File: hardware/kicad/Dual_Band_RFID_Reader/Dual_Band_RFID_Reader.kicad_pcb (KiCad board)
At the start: 2 copper layers, 74 x 74 mm, 50 parts, among them Q1 BC517, U1 Adafruit_Huzzah32, U2 LM393, U3 LM324, U4 MFRC522, Y1 Crystal

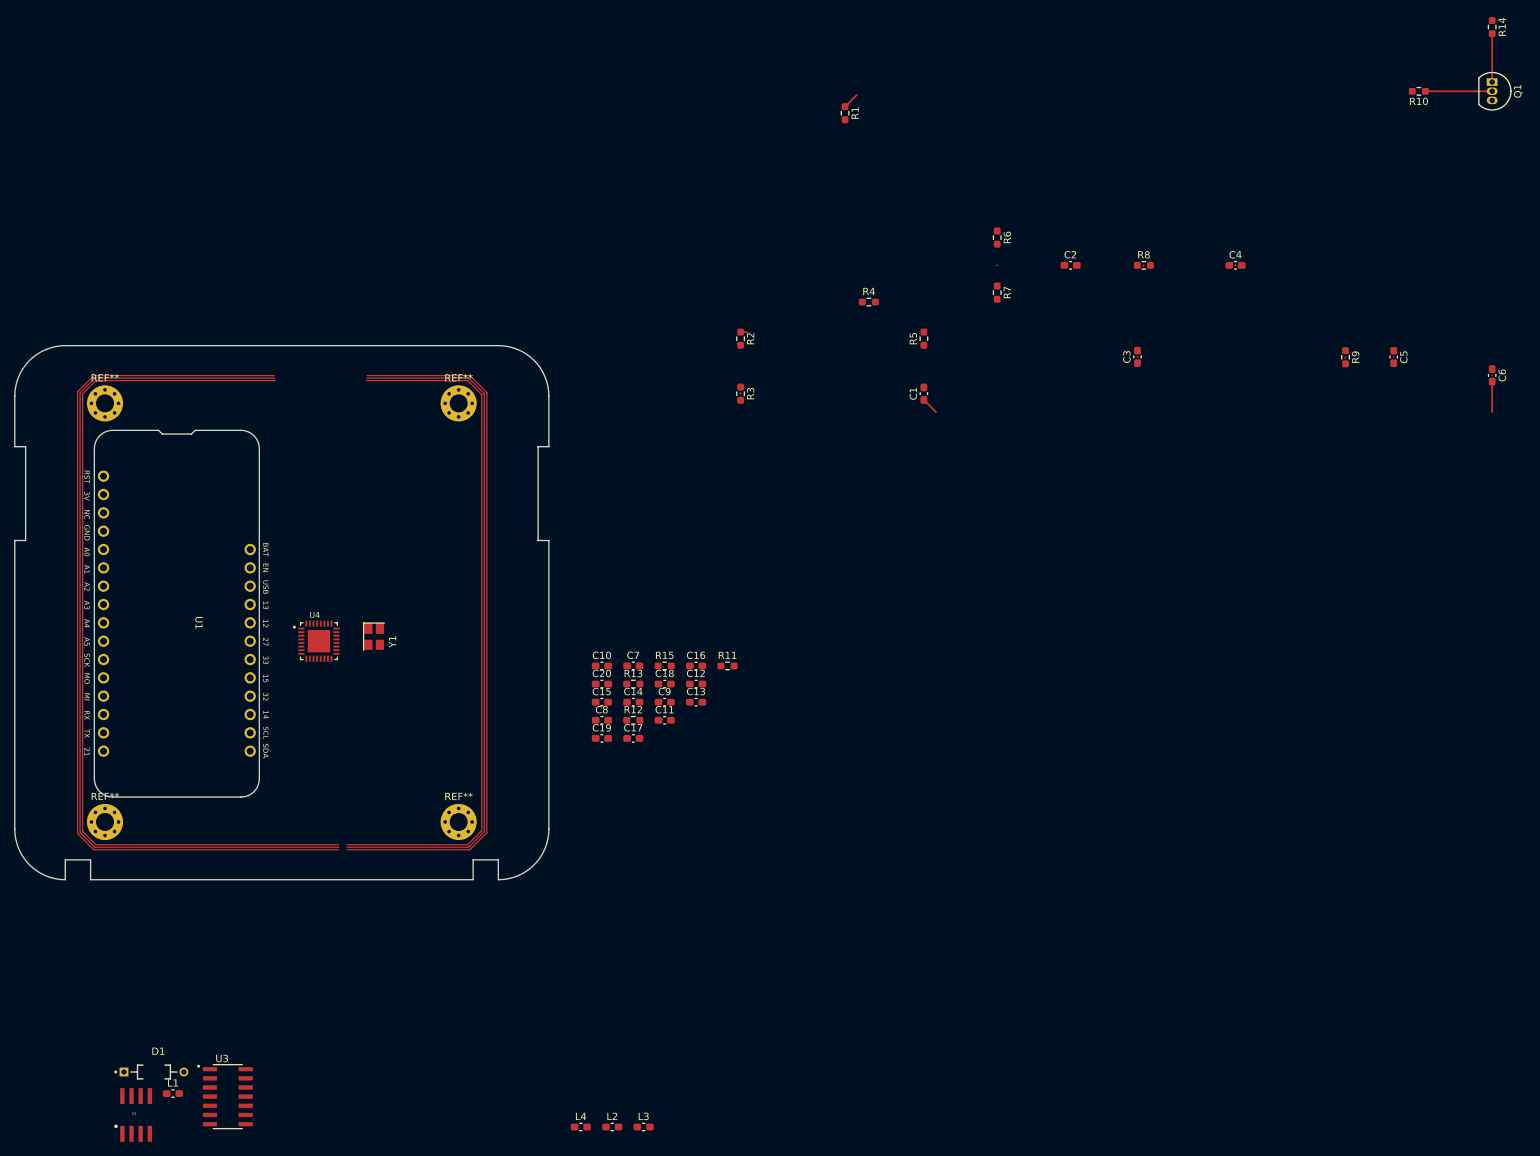
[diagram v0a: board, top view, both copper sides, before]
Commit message: Board Layout WIP
* Added correct footprint for the components that were
  producing errors
* added HF antenna trace on board periphery
* added pads for the LF antenna coil to be connected later
* corrected all the DRC errors
* completed HF layout
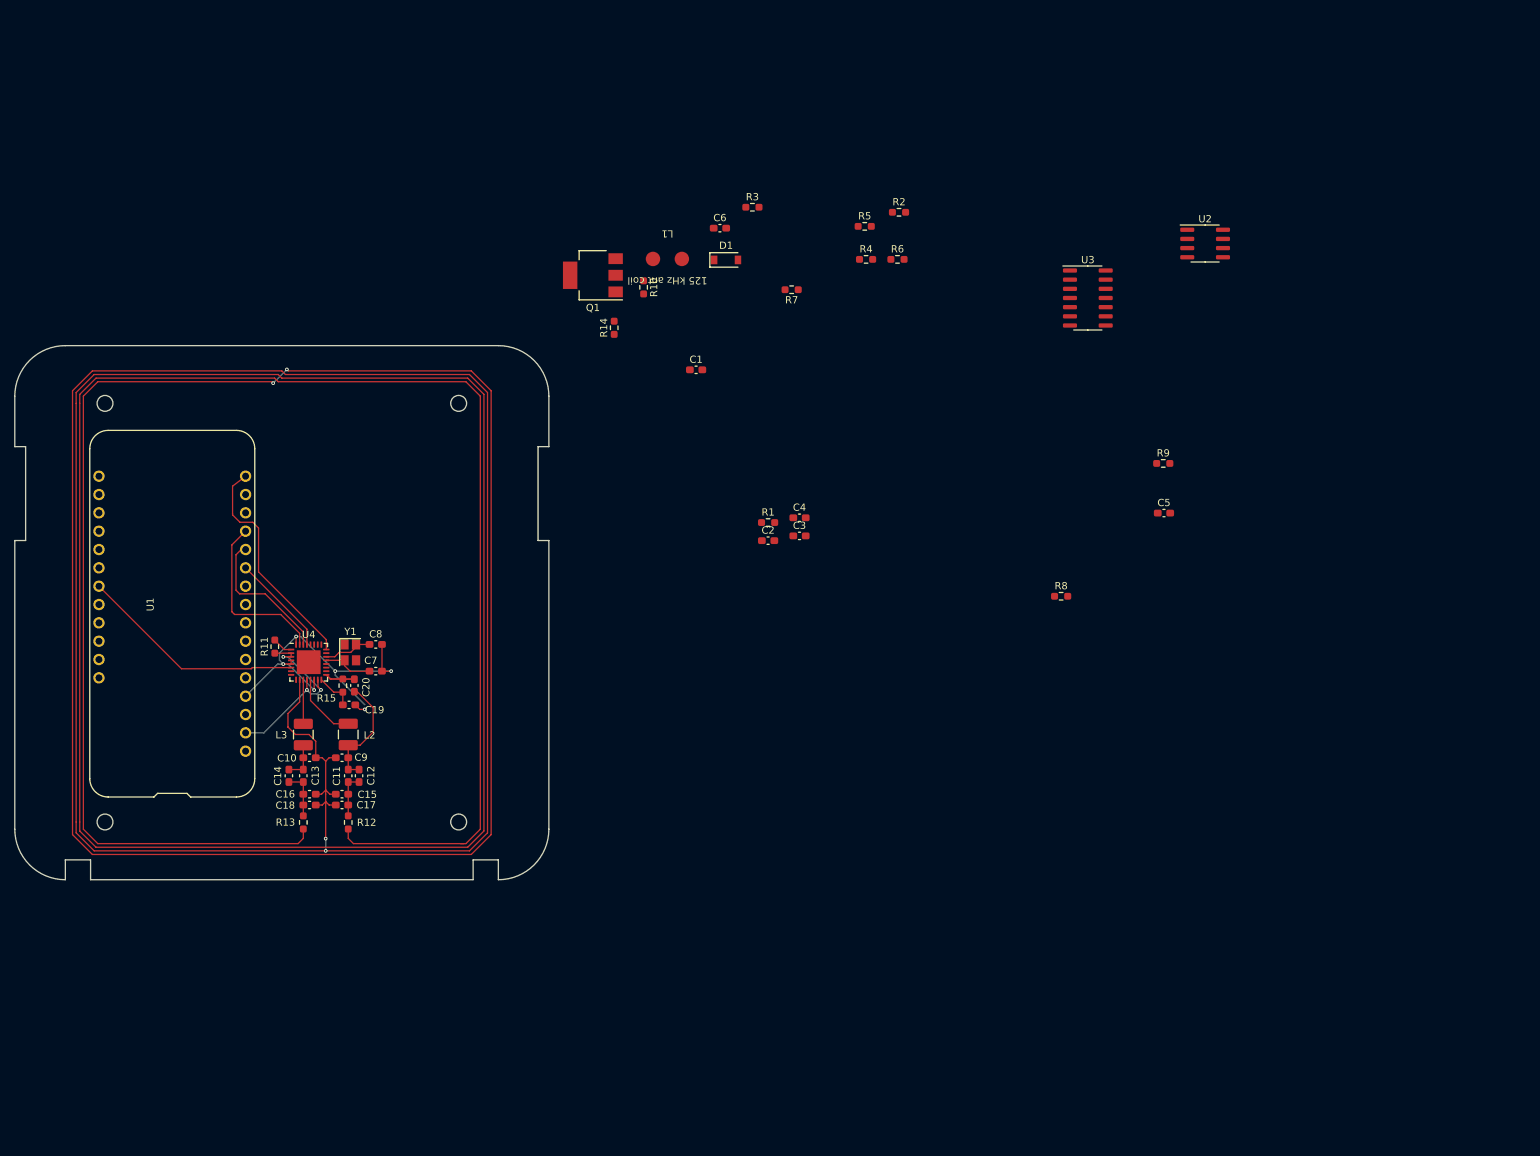
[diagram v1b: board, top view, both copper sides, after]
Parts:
- removed L4: INDUCTOR, Inductor_SMD:L_0603_1608Metric_Pad1.05x0.95mm_HandSolder
- removed the REF** at (123.5, 75.0)
- removed the REF** at (74.5, 133.0)
- removed the REF** at (123.5, 133.0)
- removed the REF** at (74.5, 75.0)
- added REF**: MountingHole_2.2mm_M2, MountingHole:MountingHole_2.2mm_M2, F.Cu at (74.5, 133.0)
- added REF**: MountingHole_2.2mm_M2, MountingHole:MountingHole_2.2mm_M2, F.Cu at (123.5, 75.0)
- added REF**: MountingHole_2.2mm_M2, MountingHole:MountingHole_2.2mm_M2, F.Cu at (123.5, 133.0)
- added REF**: MountingHole_2.2mm_M2, MountingHole:MountingHole_2.2mm_M2, F.Cu at (74.5, 75.0)
- D1: footprint ZenerDiodes:DIOAD829W49L456D191 -> Diode_SMD:D_SOD-123
- L1: footprint Inductor_SMD:L_0603_1608Metric_Pad1.05x0.95mm_HandSolder -> Capstone Footprint Lib:LF Antenna Pads
- L2, L3: footprint Inductor_SMD:L_0603_1608Metric_Pad1.05x0.95mm_HandSolder -> Inductor_SMD:L_1210_3225Metric_Pad1.42x2.65mm_HandSolder
- Q1: footprint Package_TO_SOT_THT:TO-92_Inline -> Package_TO_SOT_SMD:SOT-223
- U1: footprint Footprint Library:Adafruit Feather Huzzah 32 -> Capstone Footprint Lib:Adafruit Feather Huzzah 32
- U2: footprint DualComparator_LM393:SO08 -> Package_SO:SOIC-8_3.9x4.9mm_P1.27mm
- U3: footprint GPOPAmp_LM324:SOIC127P600X175-14N -> Package_SO:SOIC-14_3.9x8.7mm_P1.27mm
- U4: footprint MIFARE:QFN50P500X500X100-33N -> Package_DFN_QFN:QFN-32-1EP_5x5mm_P0.5mm_EP3.3x3.3mm
- Y1: footprint Footprint Library:Crystal_SMD_3225-4Pin_3.2x2.5mm_HandSoldering -> Capstone Footprint Lib:Crystal_SMD_3225-4Pin_3.2x2.5mm_HandSoldering
- moved U2 191.1 mm to (226.9, 52.9)
- moved U3 162.6 mm to (210.7, 60.4)
- moved D1 137.6 mm to (160.6, 55.1)
- moved L1 137.0 mm to (152.4, 52.0), turned to 180 degrees
- moved R14 128.6 mm to (145.1, 64.5), turned to 90 degrees
- moved Q1 127.4 mm to (142.1, 57.2), turned to 180 degrees
- moved R10 110.8 mm to (149.1, 58.9), turned to -90 degrees
- moved C6 108.9 mm to (159.7, 50.7), turned to 0 degrees
- moved L3 72.0 mm to (102.0, 120.9), turned to -90 degrees
- moved C4 69.8 mm to (170.7, 90.8)
- moved L2 65.5 mm to (108.2, 120.9), turned to -90 degrees
- moved R11 62.8 mm to (98.0, 108.7), turned to 90 degrees
- moved R1 57.7 mm to (166.4, 91.5), turned to 0 degrees
- moved C13 57.3 mm to (100.0, 126.6), turned to 90 degrees
- moved C2 56.7 mm to (166.4, 94.0)
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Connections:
- L2 pad 1: Net-(U4-TX1) -> Net-(U4-TX2)
- L3 pad 1: Net-(U4-TX2) -> Net-(U4-TX1)
- R12 pad 1: Net-(L4-Pad1) -> Net-(U4-TVSS)
- R13 pad 1: Net-(L4-Pad2) -> Net-(U4-TVSS)
- U1 pad 11: (no net) -> /High Frequency RF/SCK
- U1 pad 12: (no net) -> /High Frequency RF/MOSI
- U1 pad 13: (no net) -> /High Frequency RF/MISO
- U1 pad 14: (no net) -> /Low Frequency RF/LF_RF_RX
- U1 pad 15: (no net) -> /Low Frequency RF/LF_RF_TX
- U1 pad 16: (no net) -> /High Frequency RF/CS
- U1 pad 2: (no net) -> +3V3
- U1 pad 4: /IRQ -> GND
- U1 pad 5: /High Frequency RF/SCK -> (no net)
- Y1 pad 2: Net-(U4-OSCIN) -> (no net)
- Y1 pad 3: (no net) -> Net-(U4-OSCIN)
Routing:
- net Net-(U4-TVSS): track 0.00 -> 988.9 mm, vias 0 -> 4
- net /High Frequency RF/SCK: track 376.2 -> 14.2 mm
- net (no net): track 293.6 -> 0.00 mm
- net GND: track 6.92 -> 50.0 mm, vias 0 -> 6
- net /High Frequency RF/RST: track 0.00 -> 31.4 mm
- net /High Frequency RF/CS: track 0.00 -> 31.3 mm
- net /High Frequency RF/MISO: track 0.00 -> 24.1 mm
- net +3V3: track 3.21 -> 27.3 mm, vias 0 -> 3
- net /High Frequency RF/MOSI: track 0.00 -> 20.0 mm
- net Net-(C11-Pad2): track 0.00 -> 15.9 mm
- net Net-(U4-TX2): track 0.00 -> 9.43 mm
- net Net-(Q1-B): track 9.25 -> 0.00 mm
- net Net-(U4-OSCIN): track 0.00 -> 7.04 mm
- net Net-(U4-OSCOUT): track 0.00 -> 6.91 mm
- net Net-(Q1-C): track 6.71 -> 0.00 mm
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
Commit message: Updates traces
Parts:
- moved U2 117.0 mm to (119.9, 100.1), turned to 90 degrees
- moved C5 113.0 mm to (108.2, 88.6)
- moved R9 113.0 mm to (108.2, 86.8)
- moved U3 111.9 mm to (118.9, 124.5)
- moved R8 106.9 mm to (102.1, 80.9), turned to -90 degrees
- moved R6 91.6 mm to (116.8, 117.0), turned to 180 degrees
- moved R5 87.3 mm to (121.4, 115.5)
- moved R2 85.6 mm to (110.7, 91.9), turned to 180 degrees
- moved R4 85.2 mm to (121.4, 117.0)
- moved R7 77.1 mm to (116.8, 115.5)
- moved C4 68.9 mm to (102.1, 84.4), turned to -90 degrees
- moved R3 68.4 mm to (110.7, 90.4)
- moved C6 65.9 mm to (105.7, 88.4), turned to 90 degrees
- moved D1 64.4 mm to (107.7, 91.9), turned to 90 degrees
- moved C2 63.6 mm to (104.1, 80.9), turned to 90 degrees
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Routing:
- net /Low Frequency RF/LF_RF_RX: track 0.00 -> 78.3 mm, vias 0 -> 1
- net Net-(U3A-+): track 0.00 -> 56.9 mm, vias 0 -> 2
- net +3V3: track 27.3 -> 80.2 mm, vias 3 -> 10
- net GND: track 50.0 -> 98.4 mm
- net +5V: track 0.00 -> 39.4 mm, vias 0 -> 1
- net Net-(D1-K): track 0.00 -> 31.4 mm
- net Net-(U2A-+): track 0.00 -> 30.2 mm
- net Net-(C2-Pad2): track 0.00 -> 26.0 mm, vias 0 -> 2
- net Net-(U2A--): track 0.00 -> 23.3 mm
- net /Low Frequency RF/LF_RF_TX: track 0.00 -> 18.2 mm
- net Net-(U3A--): track 0.00 -> 9.97 mm
- net Net-(D1-A): track 0.00 -> 9.69 mm
- net Net-(Q1-C): track 0.00 -> 7.62 mm, vias 0 -> 2
- net Net-(Q1-B): track 0.00 -> 5.63 mm
- net Net-(Q1-E): track 0.00 -> 5.17 mm
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
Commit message: Updates traces_1
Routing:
- net GND: track 98.4 -> 103.3 mm
- net Net-(U2A--): track 23.3 -> 24.8 mm
- net +3V3: track 80.2 -> 81.4 mm
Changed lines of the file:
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@@
   (segment (start 112.875 112.1) (end 114.15 112.1) (width 0.1524) (layer "F.Cu") (net 1))
   (segment (start 109.8 117.4) (end 109.175 116.775) (width 0.1524) (layer "F.Cu") (net 1))
+  (segment (start 110.458987 88.614987) (end 109.066499 88.614987) (width 0.1524) (layer "F.Cu") (net 1))
   (segment (start 113.2905 108.8155) (end 112.875 108.4) (width 0.1524) (layer "F.Cu") (net 1))
   (segment (start 106.46352 90.71552) (end 106.46352 88.17552) (width 0.1524) (layer "F.Cu") (net 1))
@@
   (segment (start 109.0665 104.5915) (end 109.0665 95.504) (width 0.152) (layer "F.Cu") (net 1))
   (segment (start 115.9275 113.3875) (end 115.9275 115.470874) (width 0.1524) (layer "F.Cu") (net 1))
+  (segment (start 111.6565 89.8125) (end 110.458987 88.614987) (width 0.1524) (layer "F.Cu") (net 1))
   (segment (start 114.322711 110.213289) (end 114.15 110.386) (width 0.1524) (layer "F.Cu") (net 1))
   (segment (start 100.975 107.3) (end 100.975 108.4225) (width 0.1524) (layer "F.Cu") (net 1))
+  (segment (start 111.6565 90.424) (end 111.6565 89.8125) (width 0.1524) (layer "F.Cu") (net 1))
   (segment (start 111.252 90.424) (end 111.6565 90.424) (width 0.25) (layer "F.Cu") (net 1))
   (segment (start 100.2875 111.11) (end 99.215 111.11) (width 0.1524) (layer "F.Cu") (net 1))
@@
   (segment (start 103.475 113.2975) (end 103.475 114.725) (width 0.1524) (layer "F.Cu") (net 1))
   (segment (start 119.379999 113.942401) (end 120.5495 113.942401) (width 0.1524) (layer "F.Cu") (net 1))
+  (segment (start 106.4 112.1) (end 105.1725 112.1) (width 0.1524) (layer "F.Cu") (net 1))
   (segment (start 99.215 111.11) (end 99.2 111.125) (width 0.1524) (layer "F.Cu") (net 1))
   (segment (start 105.8175 87.5295) (end 105.664 87.5295) (width 0.25) (layer "F.Cu") (net 1))
@@
   (segment (start 108.712 91.44) (end 108.712 89.614978) (width 0.1524) (layer "F.Cu") (net 1))
   (segment (start 107.188 91.44) (end 106.46352 90.71552) (width 0.152) (layer "F.Cu") (net 1))
+  (segment (start 105.1725 112.1) (end 105.1625 112.11) (width 0.1524) (layer "F.Cu") (net 1))
   (segment (start 108.712 89.614978) (end 108.204 89.106978) (width 0.1524) (layer "F.Cu") (net 1))
   (segment (start 100.2875 110.61) (end 100.2875 111.11) (width 0.1524) (layer "F.Cu") (net 1))
@@
   (segment (start 114.189594 116.221594) (end 113.792 115.824) (width 0.1524) (layer "F.Cu") (net 11))
   (segment (start 116.983693 116.221594) (end 114.189594 116.221594) (width 0.1524) (layer "F.Cu") (net 11))
+  (segment (start 112.776 91.948) (end 111.6565 91.948) (width 0.1524) (layer "F.Cu") (net 11))
   (segment (start 109.8315 94.0835) (end 110.236 94.488) (width 0.1524) (layer "F.Cu") (net 11))
   (segment (start 113.53022 114.03822) (end 108.698478 114.03822) (width 0.1524) (layer "F.Cu") (net 11))
@@
   (segment (start 110.766711 94.002711) (end 110.766711 95.989289) (width 0.1524) (layer "F.Cu") (net 32))
   (segment (start 110.766711 95.989289) (end 110.744 96.012) (width 0.1524) (layer "F.Cu") (net 32))
+  (segment (start 109.8315 90.424) (end 109.8315 91.948) (width 0.1524) (layer "F.Cu") (net 32))
   (segment (start 109.8315 92.0515) (end 110.744 92.964) (width 0.1524) (layer "F.Cu") (net 32))
   (segment (start 110.744 93.98) (end 110.766711 94.002711) (width 0.1524) (layer "F.Cu") (net 32))

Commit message: Update traces_2
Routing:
- net +3V3: track 81.4 -> 79.6 mm, vias 10 -> 9
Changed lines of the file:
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@@
   (segment (start 98.45181 108.712) (end 97.536 108.712) (width 0.1524) (layer "F.Cu") (net 11))
   (segment (start 100.2875 109.61) (end 100.2875 110.11) (width 0.1524) (layer "F.Cu") (net 11))
-  (segment (start 101.6 102.616) (end 104.14 100.076) (width 0.1524) (layer "F.Cu") (net 11))
   (segment (start 100.2875 110.11) (end 99.215 110.11) (width 0.1524) (layer "F.Cu") (net 11))
   (segment (start 97.536 108.712) (end 97.028 108.204) (width 0.1524) (layer "F.Cu") (net 11))
@@
   (segment (start 100.2875 109.61) (end 99.34981 109.61) (width 0.1524) (layer "F.Cu") (net 11))
   (segment (start 99.215 110.11) (end 99.2 110.125) (width 0.1524) (layer "F.Cu") (net 11))
-  (segment (start 104.14 97.536) (end 104.14 97.028) (width 0.1524) (layer "F.Cu") (net 11))
   (segment (start 99.2 110.125) (end 98.5375 110.125) (width 0.1524) (layer "F.Cu") (net 11))
   (segment (start 112.776 94.488) (end 113.792 93.472) (width 0.1524) (layer "F.Cu") (net 11))
@@
   (segment (start 113.792 93.472) (end 113.792 92.456) (width 0.1524) (layer "F.Cu") (net 11))
   (segment (start 99.34981 109.61) (end 98.45181 108.712) (width 0.1524) (layer "F.Cu") (net 11))
-  (segment (start 104.14 97.028) (end 104.648 96.52) (width 0.1524) (layer "F.Cu") (net 11))
+  (segment (start 107.696 96.52) (end 101.6 102.616) (width 0.1524) (layer "F.Cu") (net 11))
   (segment (start 109.8315 93.472) (end 109.8315 94.0835) (width 0.1524) (layer "F.Cu") (net 11))
   (segment (start 98.5375 110.125) (end 98.025 109.6125) (width 0.1524) (layer "F.Cu") (net 11))
@@
   (segment (start 98.0275 109.61) (end 98.025 109.6125) (width 0.1524) (layer "F.Cu") (net 11))
   (segment (start 112.776 94.996) (end 112.776 94.488) (width 0.1524) (layer "F.Cu") (net 11))
-  (segment (start 104.14 100.076) (end 104.14 97.536) (width 0.1524) (layer "F.Cu") (net 11))
   (segment (start 97.028 108.204) (end 97.028 107.188) (width 0.1524) (layer "F.Cu") (net 11))
   (segment (start 113.284 91.948) (end 112.776 91.948) (width 0.1524) (layer "F.Cu") (net 11))
@@
   (segment (start 117.7525 116.990401) (end 116.983693 116.221594) (width 0.1524) (layer "F.Cu") (net 11))
   (segment (start 108.26322 114.473478) (end 108.26322 117.225082) (width 0.1524) (layer "F.Cu") (net 11))
-  (segment (start 104.648 96.52) (end 107.696 96.52) (width 0.1524) (layer "F.Cu") (net 11))
   (via (at 104.425 114.7) (size 0.51) (drill 0.254) (layers "F.Cu" "B.Cu") (free) (net 11))
   (via (at 110.236 94.996) (size 0.51) (drill 0.254) (layers "F.Cu" "B.Cu") (free) (net 11))
@@
   (via (at 112.776 94.996) (size 0.51) (drill 0.254) (layers "F.Cu" "B.Cu") (free) (net 11))
   (via (at 107.696 96.52) (size 0.51) (drill 0.254) (layers "F.Cu" "B.Cu") (free) (net 11))
-  (via (at 104.14 97.536) (size 0.51) (drill 0.254) (layers "F.Cu" "B.Cu") (free) (net 11))
   (via (at 99.032738 105.183262) (size 0.51) (drill 0.254) (layers "F.Cu" "B.Cu") (free) (net 11))
   (via (at 99.2 110.125) (size 0.51) (drill 0.254) (layers "F.Cu" "B.Cu") (free) (net 11))

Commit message: Update traces_3
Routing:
- net +3V3: vias 9 -> 8
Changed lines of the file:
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@@
   (via (at 110.236 94.996) (size 0.51) (drill 0.254) (layers "F.Cu" "B.Cu") (free) (net 11))
   (via (at 101.6 102.616) (size 0.51) (drill 0.254) (layers "F.Cu" "B.Cu") (free) (net 11))
-  (via (at 112.776 91.948) (size 0.51) (drill 0.254) (layers "F.Cu" "B.Cu") (free) (net 11))
   (via (at 112.776 94.996) (size 0.51) (drill 0.254) (layers "F.Cu" "B.Cu") (free) (net 11))
   (via (at 107.696 96.52) (size 0.51) (drill 0.254) (layers "F.Cu" "B.Cu") (free) (net 11))
